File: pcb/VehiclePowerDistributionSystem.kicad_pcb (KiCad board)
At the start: 4 copper layers, 70 x 70 mm, 64 parts, among them J1 B2B-XH-A, J2 B2B-XH-A, J3 B2B-XH-A, J4 B4B-XH-A, J5 B4B-XH-A, J6 B4B-XH-A, J7 B8B-XH-A, J8 B8B-XH-A, J9 B8B-XH-A, U2 D24V7F5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

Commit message: Added electrical inhibits placeholders.
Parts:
- added JP1: Jumper_2_Bridged, pcb:NPC02SXON-RC, B.Cu at (179.0, 90.0)
- added JP10: Jumper_2_Bridged, pcb:NPC02SXON-RC, B.Cu at (179.0, 110.0)
- added JP9: Jumper_2_Bridged, pcb:NPC02SXON-RC, B.Cu at (179.0, 100.0)

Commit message: Updated `VehiclePowerDistributionSystem` model.
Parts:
- removed N1: Housing, pcb:Dummy
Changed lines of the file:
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@@
 		(embedded_fonts no)
-	)
-	(footprint "pcb:Dummy"
-		(locked yes)
-		(layer "F.Cu")
-		(at 150 100)
-		(property "Reference" "N1"
-			(at 0 -0.5 0)
-			(unlocked yes)
-			(layer "F.SilkS")
-			(hide yes)
-			(effects
-				(font
-					(size 1 1)
-					(thickness 0.1)
-				)
-			)
-		)
-		(property "Value" "Housing"
-			(at 0 1 0)
-			(unlocked yes)
-			(layer "F.Fab")
-			(hide yes)
-			(effects
-				(font
-					(size 1 1)
-					(thickness 0.15)
-				)
-			)
-		)
-		(property "Datasheet" ""
-			(at 0 0 0)
-			(unlocked yes)
-			(layer "F.Fab")
-			(hide yes)
-			(effects
-				(font
-					(size 1 1)
-					(thickness 0.15)
-				)
-			)
-		)
-		(property "Description" ""
-			(at 0 0 0)
-			(unlocked yes)
-			(layer "F.Fab")
-			(hide yes)
-			(effects
-				(font
-					(size 1 1)
-					(thickness 0.15)
-				)
-			)
-		)
-		(fp_line
-			(start -1 0)
-			(end 1 0)
-			(stroke
-				(width 0.1)
-				(type default)
-			)
-			(layer "User.1")
-		)
-		(fp_line
-			(start 0 -1)
-			(end 0 1)
-			(stroke
-				(width 0.1)
-				(type default)
-			)
-			(layer "User.1")
-		)
-		(fp_circle
-			(center 0 0)
-			(end 1 0)
-			(stroke
-				(width 0.1)
-				(type default)
-			)
-			(fill no)
-			(layer "User.1")
-		)
-		(embedded_fonts no)
-		(model "${KIPRJMOD}/models/CONSat.step"
-			(opacity 0.3300)
-			(offset
-				(xyz 0 0 27.8)
-			)
-			(scale
-				(xyz 1 1 1)
-			)
-			(rotate
-				(xyz 90 -0 -0)
-			)
-		)
 	)
 	(footprint "Connector_JST:JST_XH_B4B-XH-A_1x04_P2.50mm_Vertical"

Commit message: Reverting deletion of the dummy virtual housing of `VehiclePowerDistributionSystem`.
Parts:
- added N1: Housing, pcb:Dummy, F.Cu at (150.0, 100.0)
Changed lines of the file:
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@@
 		(embedded_fonts no)
+	)
+	(footprint "pcb:Dummy"
+		(locked yes)
+		(layer "F.Cu")
+		(at 150 100)
+		(property "Reference" "N1"
+			(at 0 -0.5 0)
+			(unlocked yes)
+			(layer "F.SilkS")
+			(hide yes)
+			(effects
+				(font
+					(size 1 1)
+					(thickness 0.1)
+				)
+			)
+		)
+		(property "Value" "Housing"
+			(at 0 1 0)
+			(unlocked yes)
+			(layer "F.Fab")
+			(hide yes)
+			(effects
+				(font
+					(size 1 1)
+					(thickness 0.15)
+				)
+			)
+		)
+		(property "Datasheet" ""
+			(at 0 0 0)
+			(unlocked yes)
+			(layer "F.Fab")
+			(hide yes)
+			(effects
+				(font
+					(size 1 1)
+					(thickness 0.15)
+				)
+			)
+		)
+		(property "Description" ""
+			(at 0 0 0)
+			(unlocked yes)
+			(layer "F.Fab")
+			(hide yes)
+			(effects
+				(font
+					(size 1 1)
+					(thickness 0.15)
+				)
+			)
+		)
+		(fp_line
+			(start -1 0)
+			(end 1 0)
+			(stroke
+				(width 0.1)
+				(type default)
+			)
+			(layer "User.1")
+		)
+		(fp_line
+			(start 0 -1)
+			(end 0 1)
+			(stroke
+				(width 0.1)
+				(type default)
+			)
+			(layer "User.1")
+		)
+		(fp_circle
+			(center 0 0)
+			(end 1 0)
+			(stroke
+				(width 0.1)
+				(type default)
+			)
+			(fill no)
+			(layer "User.1")
+		)
+		(embedded_fonts no)
+		(model "${KIPRJMOD}/models/CONSat.step"
+			(opacity 0.3300)
+			(offset
+				(xyz 0 0 27.8)
+			)
+			(scale
+				(xyz 1 1 1)
+			)
+			(rotate
+				(xyz 90 -0 -0)
+			)
+		)
 	)
 	(footprint "Connector_JST:JST_XH_B4B-XH-A_1x04_P2.50mm_Vertical"

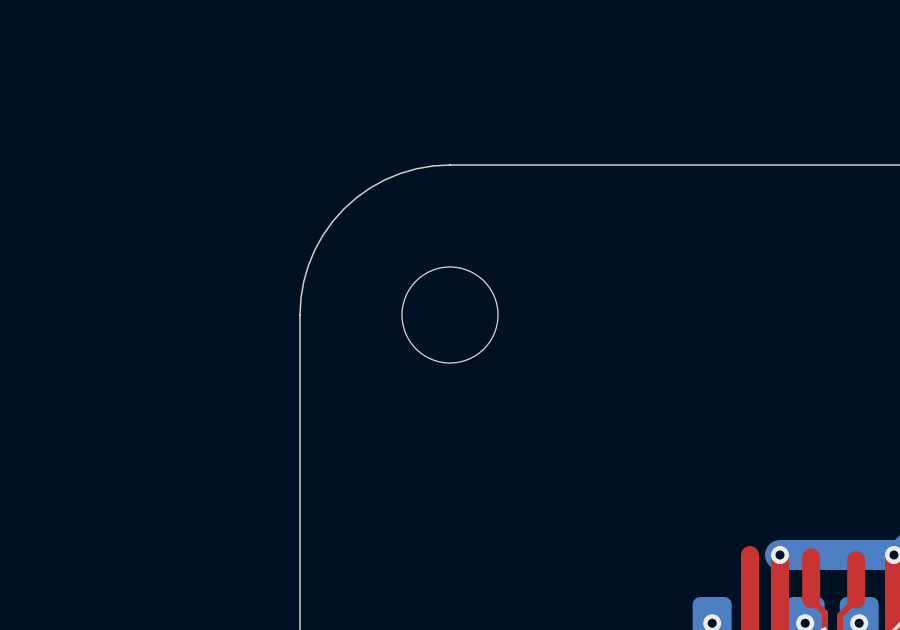
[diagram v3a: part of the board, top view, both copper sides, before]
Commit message: Made one of the mounting holes be optionally tied to ground.
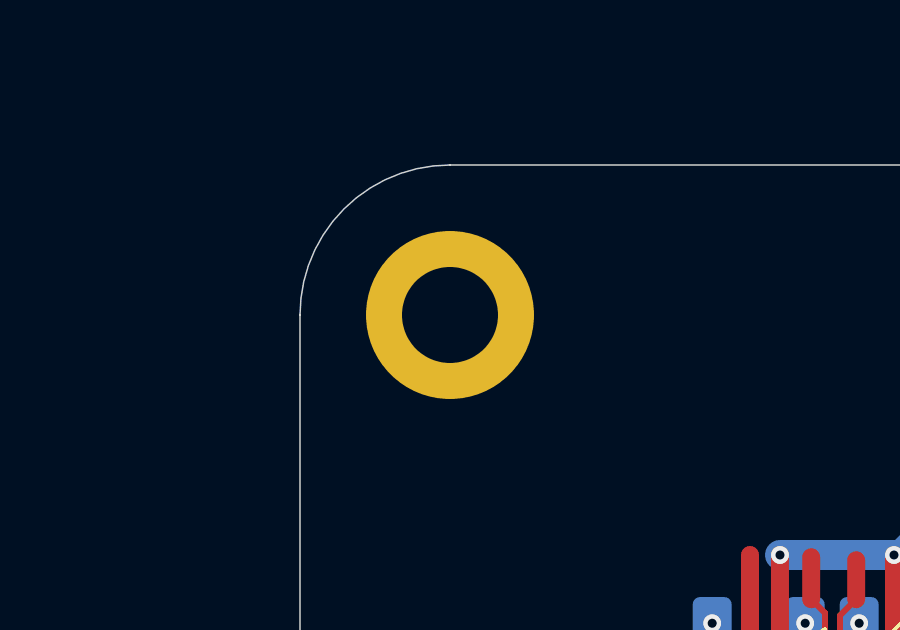
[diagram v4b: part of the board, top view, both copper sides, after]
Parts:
- H1: value MountingHole -> MountingHole_Pad; footprint MountingHole:MountingHole_3.2mm_M3 -> MountingHole:MountingHole_3.2mm_M3_DIN965_Pad
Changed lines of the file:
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@@
 	(net 78 "unconnected-(JP10-A-Pad1)")
 	(net 79 "unconnected-(JP10-B-Pad2)")
+	(net 80 "Net-(JP11-B)")
 	(footprint "LED_SMD:LED_1206_3216Metric_Pad1.42x1.75mm_HandSolder"
 		(layer "F.Cu")
@@
 		)
 	)
-	(footprint "MountingHole:MountingHole_3.2mm_M3"
+	(footprint "MountingHole:MountingHole_3.2mm_M3_DIN965_Pad"
 		(locked yes)
 		(layer "F.Cu")
 		(at 120 70)
-		(descr "Mounting Hole 3.2mm, M3, no annular, generated by kicad-footprint-generator mountinghole.py")
-		(tags "mountinghole M3")
+		(descr "Mounting Hole 3.2mm, M3, generated by kicad-footprint-generator mountinghole.py")
+		(tags "mountinghole M3 DIN965")
 		(property "Reference" "H1"
-			(at 0 -4.15 0)
-			(layer "F.SilkS")
-			(hide yes)
-			(effects
-				(font
-					(size 1 1)
-					(thickness 0.15)
-				)
-			)
-		)
-		(property "Value" "MountingHole"
-			(at 0 4.15 0)
+			(at 0 -3.75 0)
+			(layer "F.SilkS")
+			(hide yes)
+			(effects
+				(font
+					(size 1 1)
+					(thickness 0.15)
+				)
+			)
+		)
+		(property "Value" "MountingHole_Pad"
+			(at 0 3.75 0)
 			(layer "F.Fab")
 			(effects
@@
 			)
 		)
-		(property "Description" "Mounting Hole without connection"
+		(property "Description" "Mounting Hole with connection"
 			(at 0 0 0)
 			(layer "F.Fab")
@@
 			)
 		)
-		(property ki_fp_filters "MountingHole*")
+		(property ki_fp_filters "MountingHole*Pad*")
 		(sheetname "/")
 		(sheetfile "VehiclePowerDistributionSystem.kicad_sch")
@@
 		(fp_circle
 			(center 0 0)
-			(end 3.2 0)
+			(end 2.8 0)
 			(stroke
 				(width 0.15)
@@
 		(fp_circle
 			(center 0 0)
-			(end 3.45 0)
+			(end 3.05 0)
 			(stroke
 				(width 0.05)
@@
 			)
 		)
-		(pad "" np_thru_hole circle
+		(pad "1" thru_hole circle
 			(at 0 0)
-			(size 3.2 3.2)
+			(size 5.6 5.6)
 			(drill 3.2)
 			(layers "*.Cu" "*.Mask")
+			(remove_unused_layers no)
+			(net 80 "Net-(JP11-B)")
+			(pinfunction "1")
+			(pintype "input")
+			(zone_connect 2)
 		)
 		(embedded_fonts no)

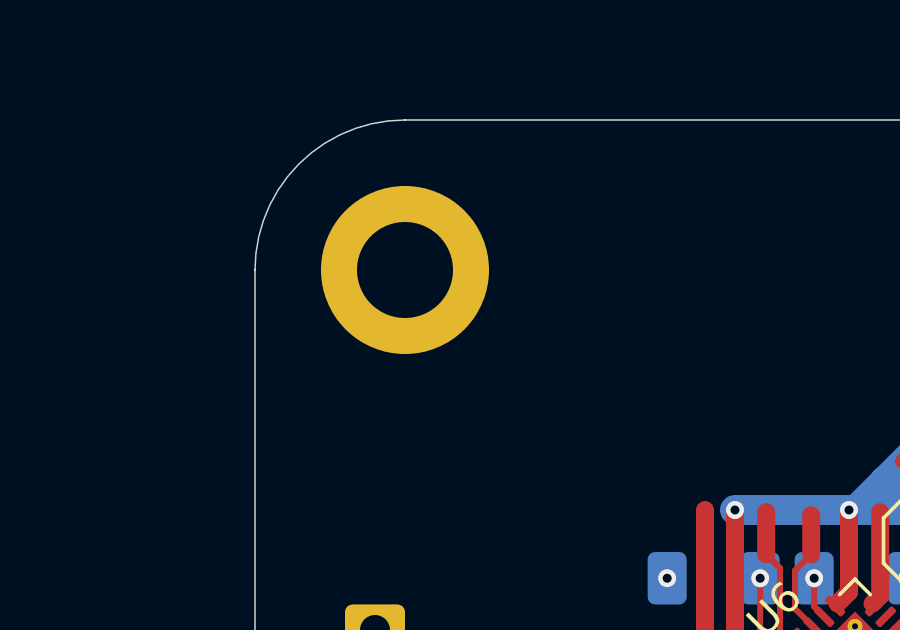
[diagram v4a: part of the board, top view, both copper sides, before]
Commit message: Added asymmetry in mounting hole placement for `VehiclePowerDistributionSystem`.
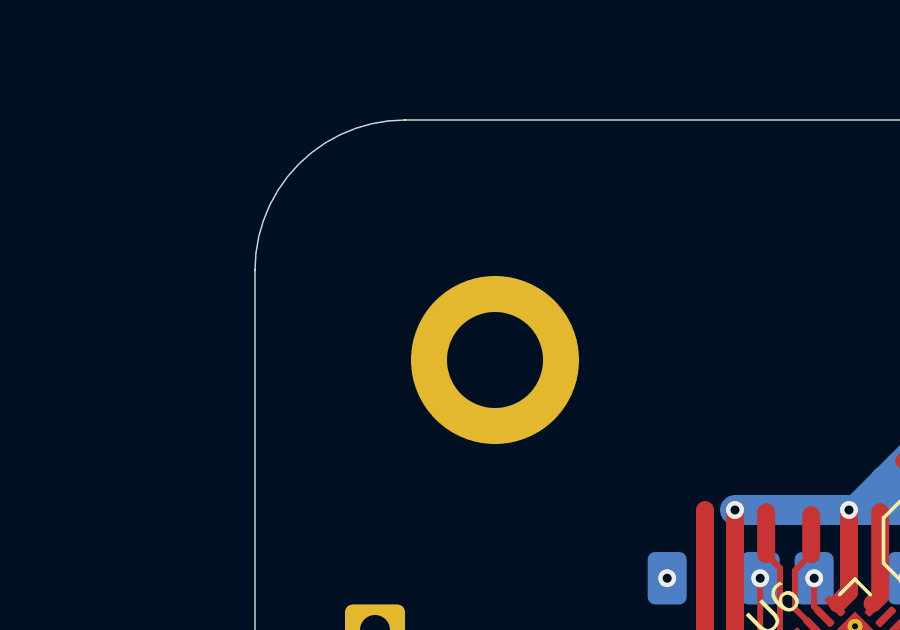
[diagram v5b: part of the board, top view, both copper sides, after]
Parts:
- moved H1 4.24 mm to (123.0, 73.0)
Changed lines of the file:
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@@
 		(locked yes)
 		(layer "F.Cu")
-		(at 120 70)
+		(at 123 73)
 		(descr "Mounting Hole 3.2mm, M3, generated by kicad-footprint-generator mountinghole.py")
 		(tags "mountinghole M3 DIN965")

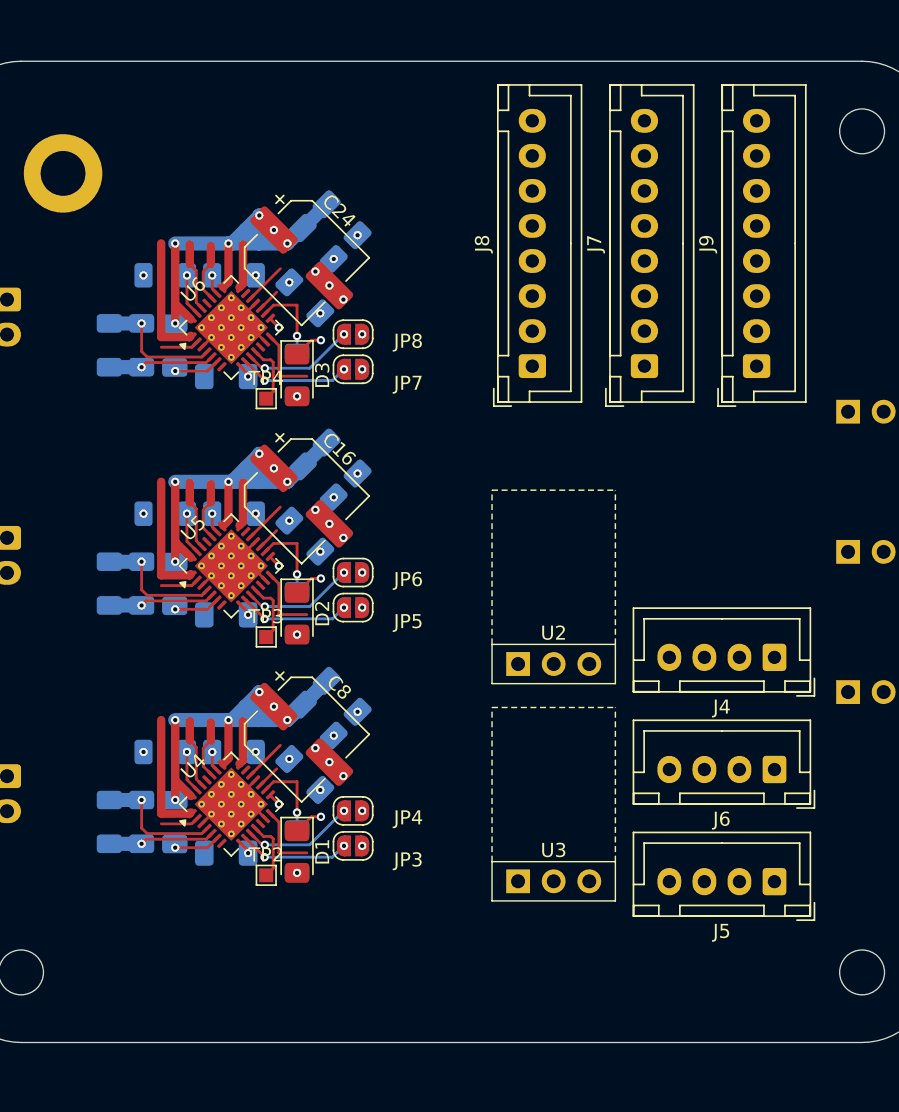
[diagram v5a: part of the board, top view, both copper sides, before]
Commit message: Using 24-pin ribbon connector for I/O on `VehiclePowerDistributionSystem`.
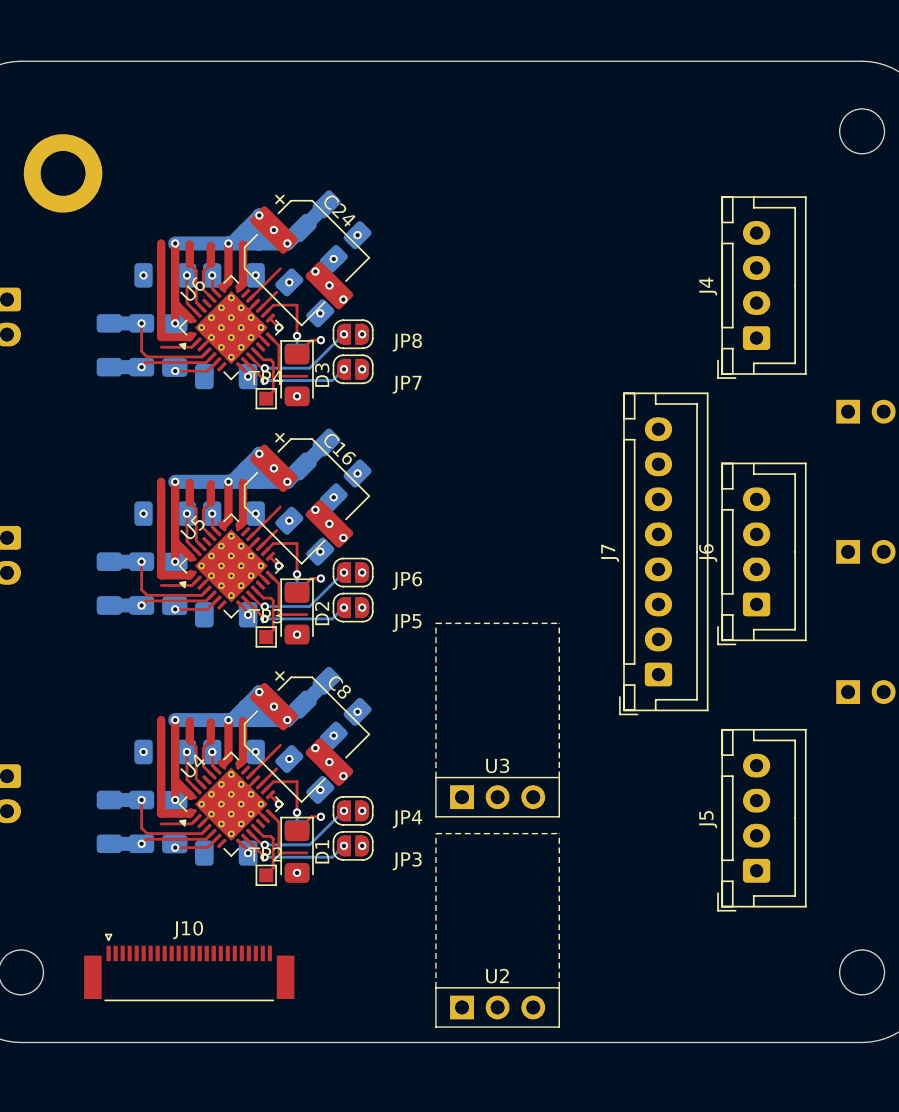
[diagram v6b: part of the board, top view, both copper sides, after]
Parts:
- removed J8, J9: B8B-XH-A, Connector_JST:JST_XH_B8B-XH-A_1x08_P2.50mm_Vertical
- added J10: FFC2B28-24-G, pcb:Flat Flexible Cable 24-Pin 0.5mm Connector, F.Cu at (132.0, 130.0)
- moved U2 24.8 mm to (154.0, 132.5)
- moved J4 22.8 mm to (172.5, 84.8), turned to 90 degrees
- moved J7 22.0 mm to (165.5, 108.8)
- moved J6 11.8 mm to (172.5, 103.8), turned to 90 degrees
- moved U3 7.21 mm to (154.0, 117.5)
- moved J5 1.49 mm to (172.5, 122.8), turned to 90 degrees

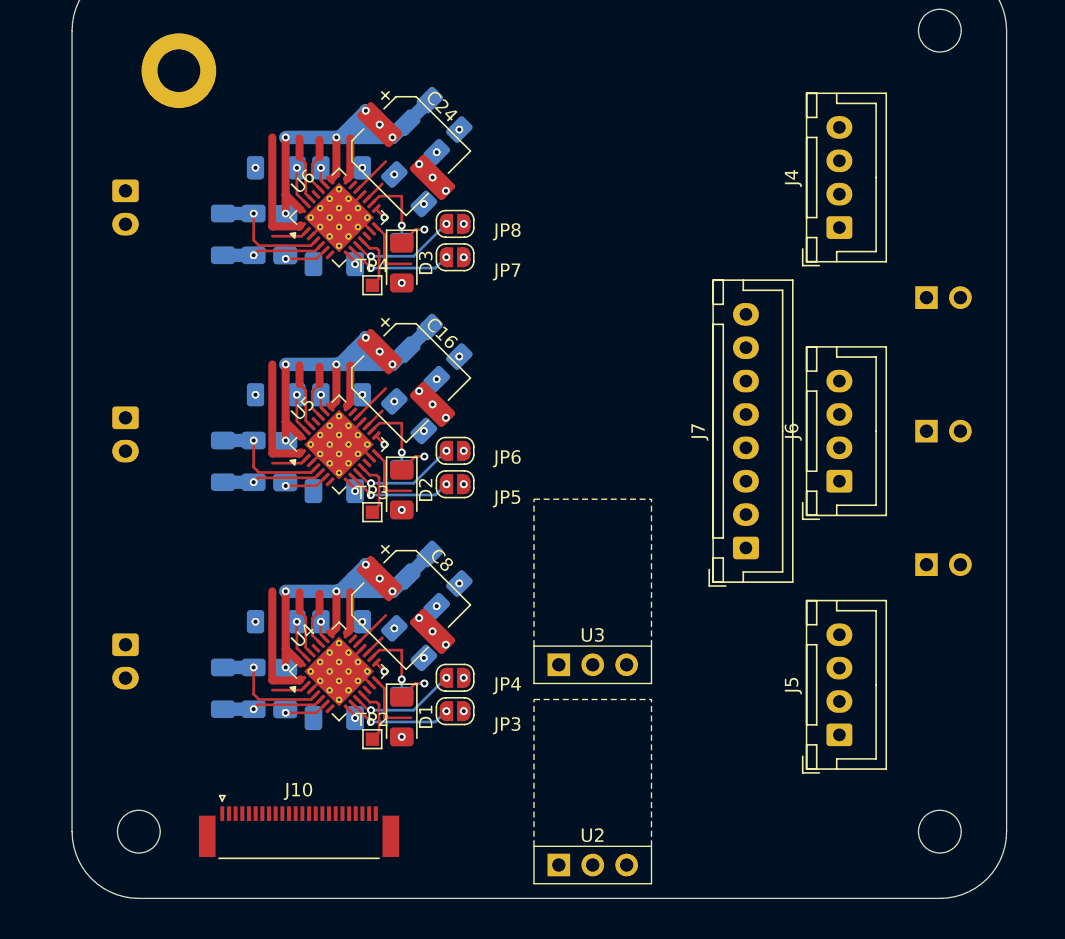
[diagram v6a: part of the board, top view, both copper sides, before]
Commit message: Repositioned the vehicle PDS I/O connector.
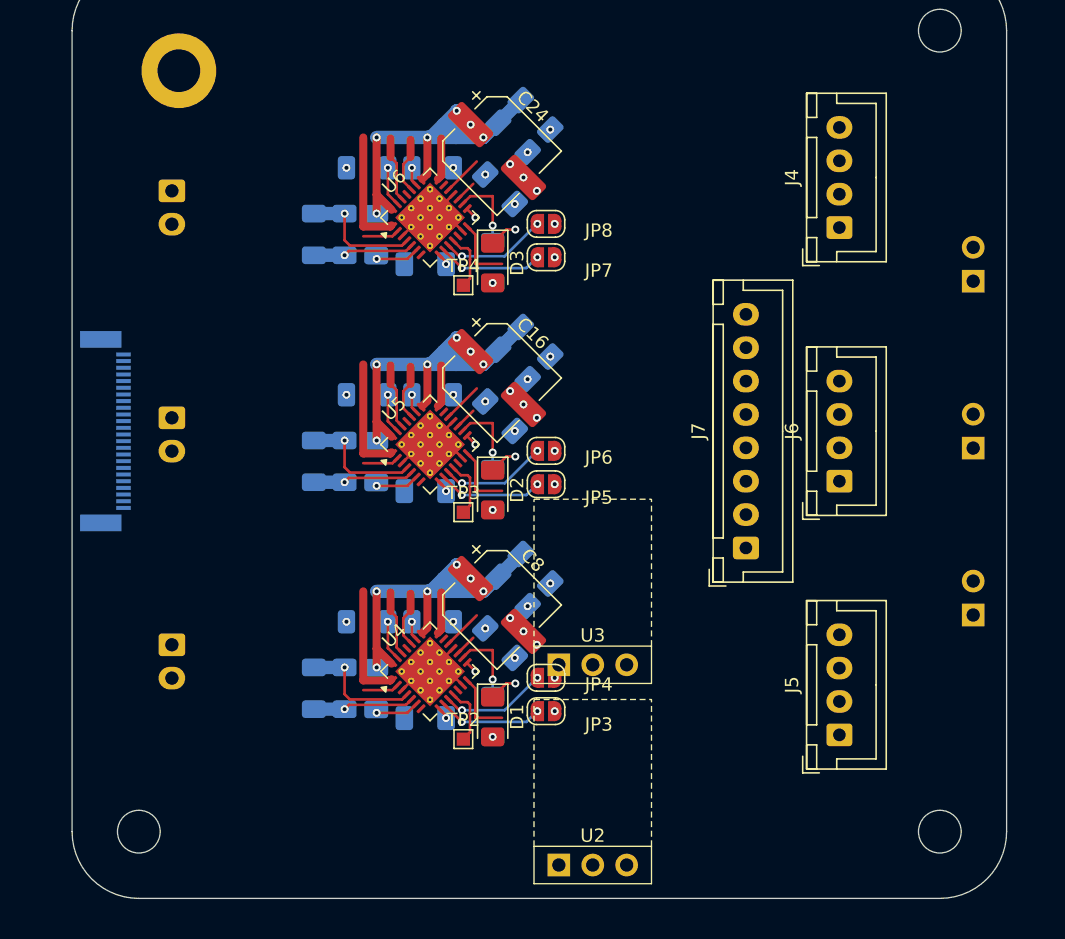
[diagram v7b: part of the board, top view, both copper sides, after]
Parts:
- J10: moved to B.Cu
- moved J10 33.3 mm to (117.5, 100.0), turned to 90 degrees
- moved C11 6.81 mm to (133.1, 102.3)
- moved C21 6.81 mm to (133.1, 85.3)
- moved C3 6.81 mm to (133.1, 119.3)
- moved C1 6.81 mm to (147.1, 115.9)
- moved C10 6.81 mm to (137.8, 102.3)
- moved C12 6.81 mm to (141.4, 104.5)
- moved C13 6.81 mm to (135.4, 102.3)
- moved C14 6.81 mm to (149.7, 93.3)
- moved C15 6.81 mm to (148.0, 95.0)
- moved C16 6.81 mm to (146.8, 96.0)
- moved C17 6.81 mm to (147.1, 81.9)
- moved C18 6.81 mm to (137.8, 85.3)
- moved C19 6.81 mm to (135.4, 85.3)
- moved C2 6.81 mm to (137.8, 119.3)
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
